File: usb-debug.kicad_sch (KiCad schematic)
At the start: 78 parts, among them IC15 TPS7A0518PDBVT, IC16 AP22653W6-7, IC7 HD3SS3220, J11 632723300011, Q1 PMV32UP, T6 BSS138APW, T7 BSS138APW

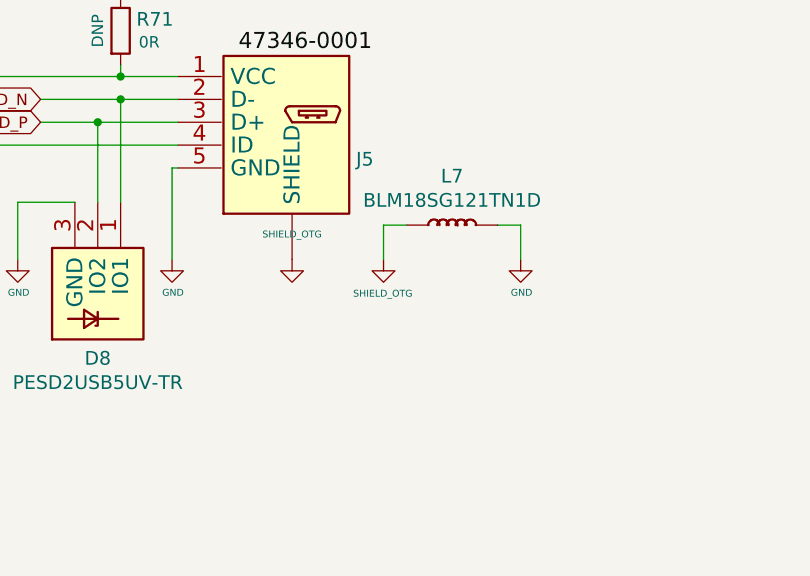
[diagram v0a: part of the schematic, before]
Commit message: Fixed schematic connection between USB OTG shield and L7
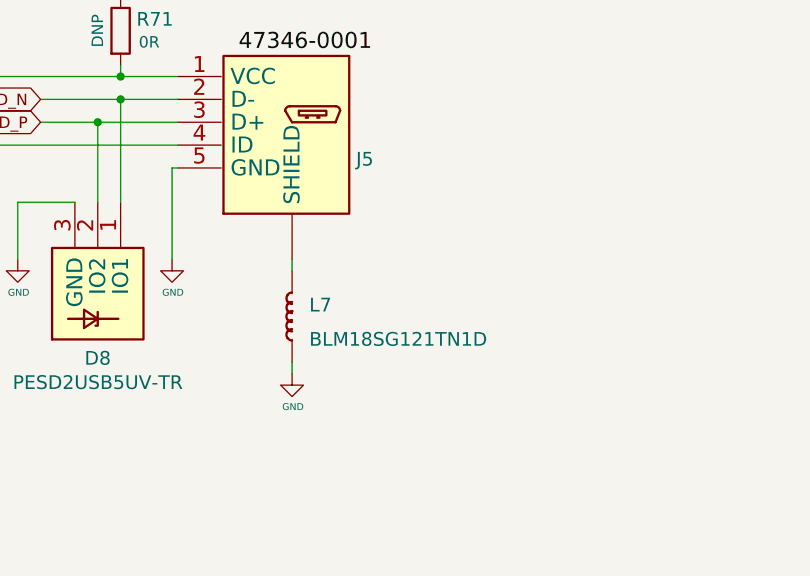
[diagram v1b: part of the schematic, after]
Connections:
- net GND: no longer J5.S (SHIELD), L7.2 (P)
- new net: J5.S (SHIELD), L7.2 (P)
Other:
- moved on the sheet: L7
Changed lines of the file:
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@@
     (stroke (width 0) (type default) (color 0 0 0 0))
   )
+  (wire (pts (xy 222.885 184.15) (xy 222.885 182.88))
+    (stroke (width 0) (type default) (color 0 0 0 0))
+  )
   (wire (pts (xy 192.405 165.1) (xy 192.405 171.45))
     (stroke (width 0) (type default) (color 0 0 0 0))
@@
     (stroke (width 0) (type default) (color 0 0 0 0))
   )
-  (wire (pts (xy 245.745 167.64) (xy 248.285 167.64))
-    (stroke (width 0) (type default) (color 0 0 0 0))
-  )
   (wire (pts (xy 151.13 50.8) (xy 151.13 58.42))
     (stroke (width 0) (type default) (color 0 0 0 0))
@@
     (stroke (width 0) (type default) (color 0 0 0 0))
   )
+  (wire (pts (xy 222.885 172.72) (xy 222.885 171.45))
+    (stroke (width 0) (type default) (color 0 0 0 0))
+  )
   (wire (pts (xy 222.25 261.62) (xy 222.25 258.445))
     (stroke (width 0) (type default) (color 0 0 0 0))
@@
     (stroke (width 0) (type default) (color 0 0 0 0))
   )
-  (wire (pts (xy 235.585 167.64) (xy 233.045 167.64))
-    (stroke (width 0) (type default) (color 0 0 0 0))
-  )
   (wire (pts (xy 290.195 86.995) (xy 290.195 59.055))
     (stroke (width 0) (type default) (color 0 0 0 0))
@@
     (stroke (width 0) (type default) (color 0 0 0 0))
   )
-  (wire (pts (xy 233.045 167.64) (xy 233.045 171.45))
-    (stroke (width 0) (type default) (color 0 0 0 0))
-  )
   (wire (pts (xy 102.235 244.475) (xy 102.235 227.965))
     (stroke (width 0) (type default) (color 0 0 0 0))
@@
     (stroke (width 0) (type default) (color 0 0 0 0))
   )
-  (wire (pts (xy 248.285 167.64) (xy 248.285 171.45))
-    (stroke (width 0) (type default) (color 0 0 0 0))
-  )
   (wire (pts (xy 42.545 165.1) (xy 42.545 166.37))
     (stroke (width 0) (type default) (color 0 0 0 0))
@@
     (pin "1")
   )
-  (symbol (lib_id "jetson-nano-baseboard:BLM18SG121TN1D") (at 240.665 167.64 0) (unit 1)
-    (in_bom yes) (on_board yes)
-    (property "Reference" "L7" (id 0) (at 240.665 162.2044 0)
-      (effects (font (size 1.524 1.524)))
+  (symbol (lib_id "jetson-nano-baseboard:BLM18SG121TN1D") (at 222.885 177.8 90) (unit 1)
+    (in_bom yes) (on_board yes) (fields_autoplaced)
+    (property "Reference" "L7" (id 0) (at 224.79 176.5298 90)
+      (effects (font (size 1.524 1.524)) (justify right))
     )
-    (property "Value" "BLM18SG121TN1D" (id 1) (at 240.665 164.8968 0)
-      (effects (font (size 1.524 1.524)))
+    (property "Value" "BLM18SG121TN1D" (id 1) (at 224.79 180.3398 90)
+      (effects (font (size 1.524 1.524)) (justify right))
     )
-    (property "Footprint" "jetson-nano-baseboard-footprints:0603" (id 2) (at 233.045 165.1 0)
+    (property "Footprint" "jetson-nano-baseboard-footprints:0603" (id 2) (at 220.345 185.42 0)
       (effects (font (size 1.524 1.524)) hide)
     )
-    (property "Datasheet" "" (id 3) (at 233.045 165.1 0)
+    (property "Datasheet" "" (id 3) (at 220.345 185.42 0)
       (effects (font (size 1.524 1.524)) hide)
     )
-    (property "Manufacturer" "Murata" (id 4) (at 154.305 380.8222 90)
+    (property "Manufacturer" "Murata" (id 4) (at 436.0672 264.16 90)
       (effects (font (size 1.524 1.524)) hide)
     )
-    (property "MPN" "BLM18SG121TN1D" (id 5) (at -665.3784 673.227 0)
+    (property "MPN" "BLM18SG121TN1D" (id 5) (at 728.472 1083.8434 0)
       (effects (font (size 1.27 1.27)) hide)
     )
@@
     (pin "1")
   )
-  (symbol (lib_id "jetson-nano-baseboard:GND") (at 222.885 171.45 0) (unit 1)
-    (in_bom yes) (on_board yes)
-    (property "Reference" "#SHIELD_OTG_02" (id 0) (at 222.885 167.894 0)
-      (effects (font (size 0.508 0.508)) hide)
-    )
-    (property "Value" "SHIELD_OTG" (id 1) (at 222.885 168.656 0)
-      (effects (font (size 0.762 0.762)))
-    )
-    (property "Footprint" "" (id 2) (at 222.885 171.45 0)
-      (effects (font (size 1.778 1.778)) hide)
-    )
-    (property "Datasheet" "" (id 3) (at 222.885 171.45 0)
-      (effects (font (size 1.778 1.778)) hide)
-    )
-    (pin "1")
-  )
-  (symbol (lib_id "jetson-nano-baseboard:GND") (at 248.285 171.45 0) (unit 1)
-    (in_bom yes) (on_board yes)
-    (property "Reference" "#GND_0107" (id 0) (at 248.285 171.45 0)
-      (effects (font (size 0.508 0.508)) hide)
-    )
-    (property "Value" "GND" (id 1) (at 248.3866 175.133 0)
-      (effects (font (size 0.762 0.762)))
-    )
-    (property "Footprint" "" (id 2) (at 248.285 171.45 0)
-      (effects (font (size 1.778 1.778)) hide)
-    )
-    (property "Datasheet" "" (id 3) (at 248.285 171.45 0)
-      (effects (font (size 1.778 1.778)) hide)
-    )
-    (pin "1")
-  )
-  (symbol (lib_id "jetson-nano-baseboard:GND") (at 233.045 171.45 0) (unit 1)
+  (symbol (lib_id "jetson-nano-baseboard:GND") (at 222.885 184.15 0) (unit 1)
     (in_bom yes) (on_board yes)
-    (property "Reference" "#SHIELD_OTG01" (id 0) (at 233.045 167.894 0)
+    (property "Reference" "#GND_0107" (id 0) (at 222.885 184.15 0)
       (effects (font (size 0.508 0.508)) hide)
     )
-    (property "Value" "SHIELD_OTG" (id 1) (at 232.9688 175.2346 0)
+    (property "Value" "GND" (id 1) (at 222.9866 187.833 0)
       (effects (font (size 0.762 0.762)))
     )
-    (property "Footprint" "" (id 2) (at 233.045 171.45 0)
+    (property "Footprint" "" (id 2) (at 222.885 184.15 0)
       (effects (font (size 1.778 1.778)) hide)
     )
-    (property "Datasheet" "" (id 3) (at 233.045 171.45 0)
+    (property "Datasheet" "" (id 3) (at 222.885 184.15 0)
       (effects (font (size 1.778 1.778)) hide)
     )

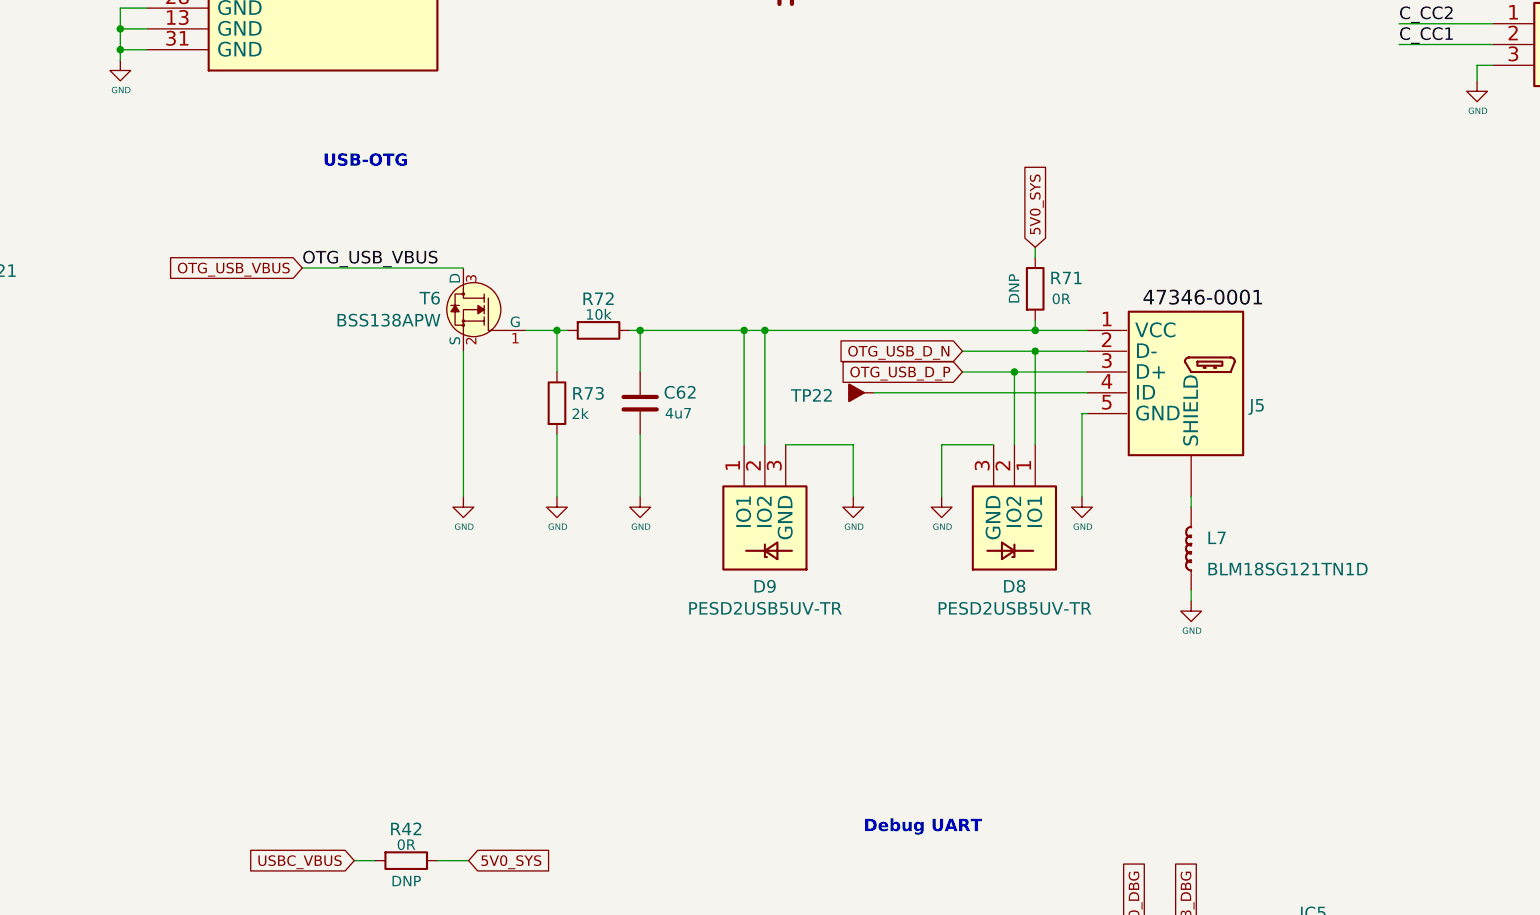
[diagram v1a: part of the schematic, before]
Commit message: Added USB OTG functionality
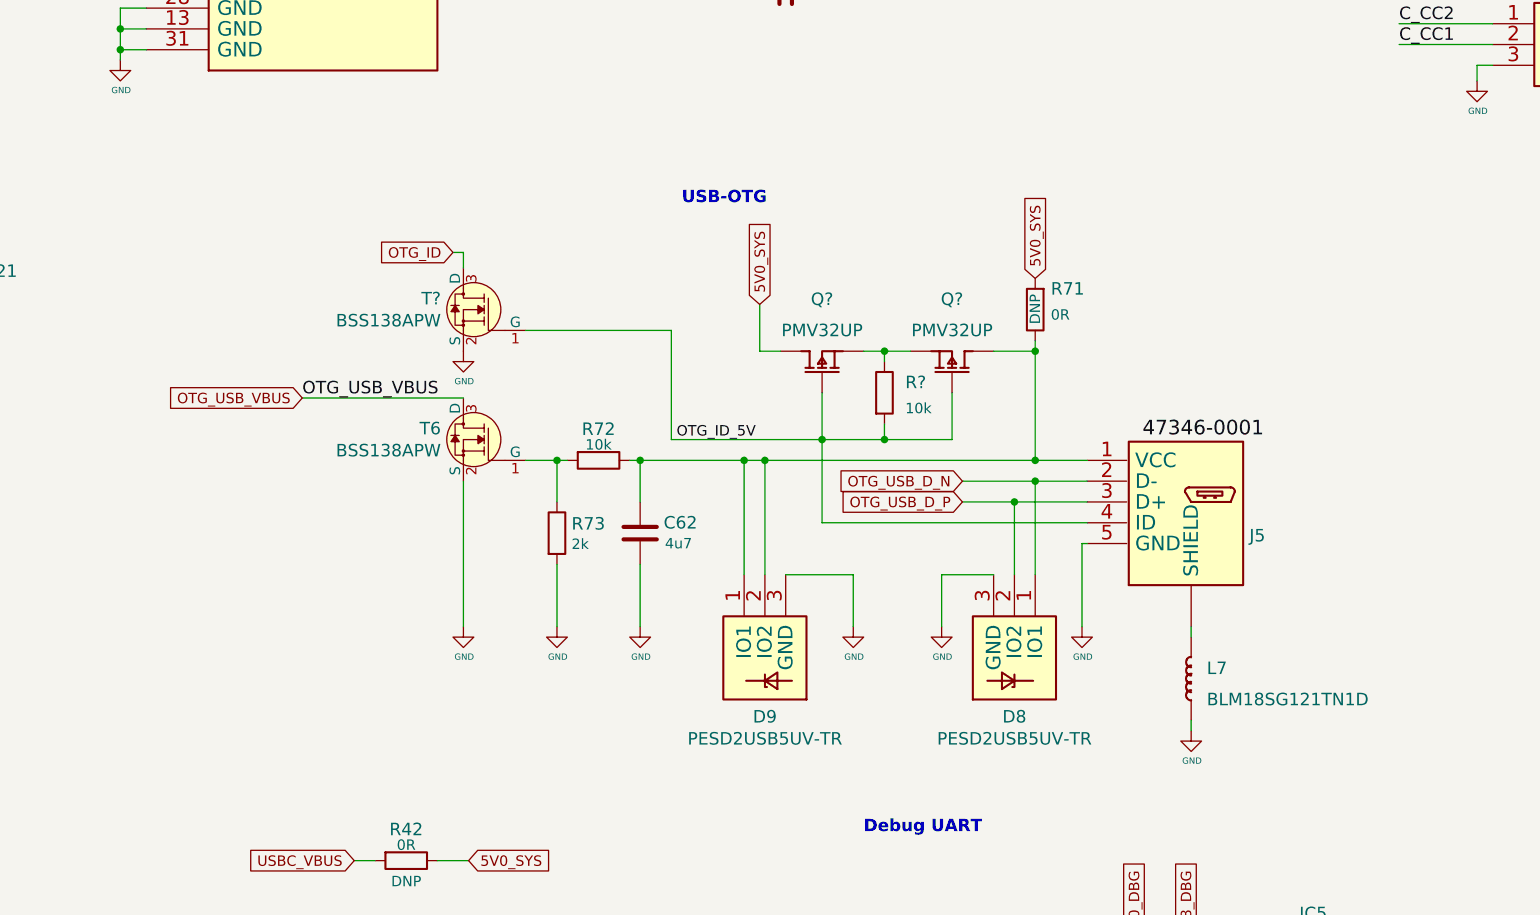
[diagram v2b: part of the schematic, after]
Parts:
- removed TP22: ~, jetson-nano-baseboard-footprints:TP-R-1.5, symbol jetson-nano-baseboard:Testpad
- added Q? (x2): PMV32UP, jetson-nano-baseboard-footprints:SOT-23s, symbol jetson-nano-baseboard:PMOS
- added R?: R_10k_0402, jetson-nano-baseboard-footprints:0402-res, symbol jetson-nano-baseboard:R_10k_0402
- added T?: BSS138APW, jetson-nano-baseboard-footprints:SC70-3, symbol jetson-nano-baseboard:BSS138APW
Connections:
- net 5V0_SYS: now also R71.2, Q?.3 (D); no longer R71.1
- net GND: now also T?.2 (S)
- net OTG_ID_5V: now reaches J5.4 (ID)
- net OTG_ID_5V: now also Q?.1 (G), Q?.1 (G), R?.2, T?.1 (G)
- net at C62.2, D9.1 (IO1), D9.2 (IO2)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: now also R71.1, Q?.3 (D); no longer R71.2
- new net: Q?.2 (S), Q?.2 (S), R?.1
- new net OTG_ID: T?.3 (D)
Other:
- moved on the sheet: C62, D8, D9, J5, L7, R71, R72, R73, T6

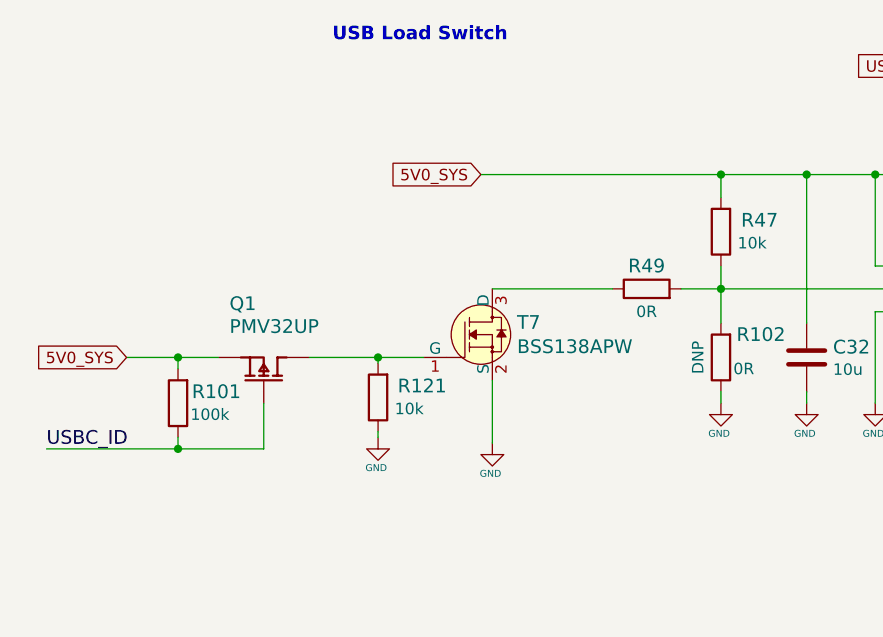
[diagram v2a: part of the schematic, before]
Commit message: Modified USBC ID logic
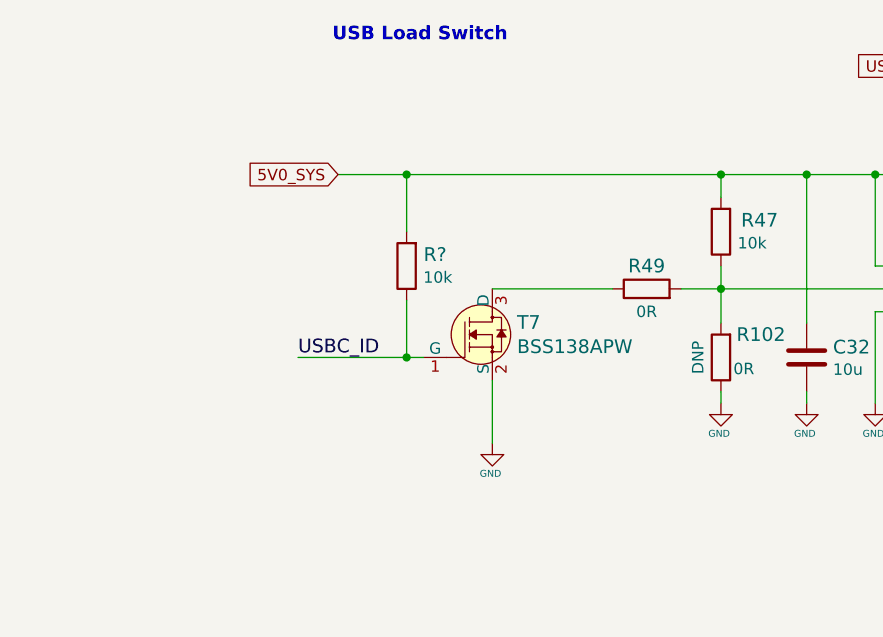
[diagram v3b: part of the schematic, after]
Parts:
- removed Q1: PMV32UP, jetson-nano-baseboard-footprints:SOT-23s, symbol jetson-nano-baseboard:PMOS
- removed R101: R_100k_0402, jetson-nano-baseboard-footprints:0402-res, symbol jetson-nano-baseboard:R_100k_0402
- removed R121: R_10k_0402, jetson-nano-baseboard-footprints:0402-res, symbol jetson-nano-baseboard:R_10k_0402
- added R?: R_10k_0402, jetson-nano-baseboard-footprints:0402-res, symbol jetson-nano-baseboard:R_10k_0402
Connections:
- net 5V0_SYS: now also R?.2
- net USBC_ID: now also T7.1 (G), R?.1

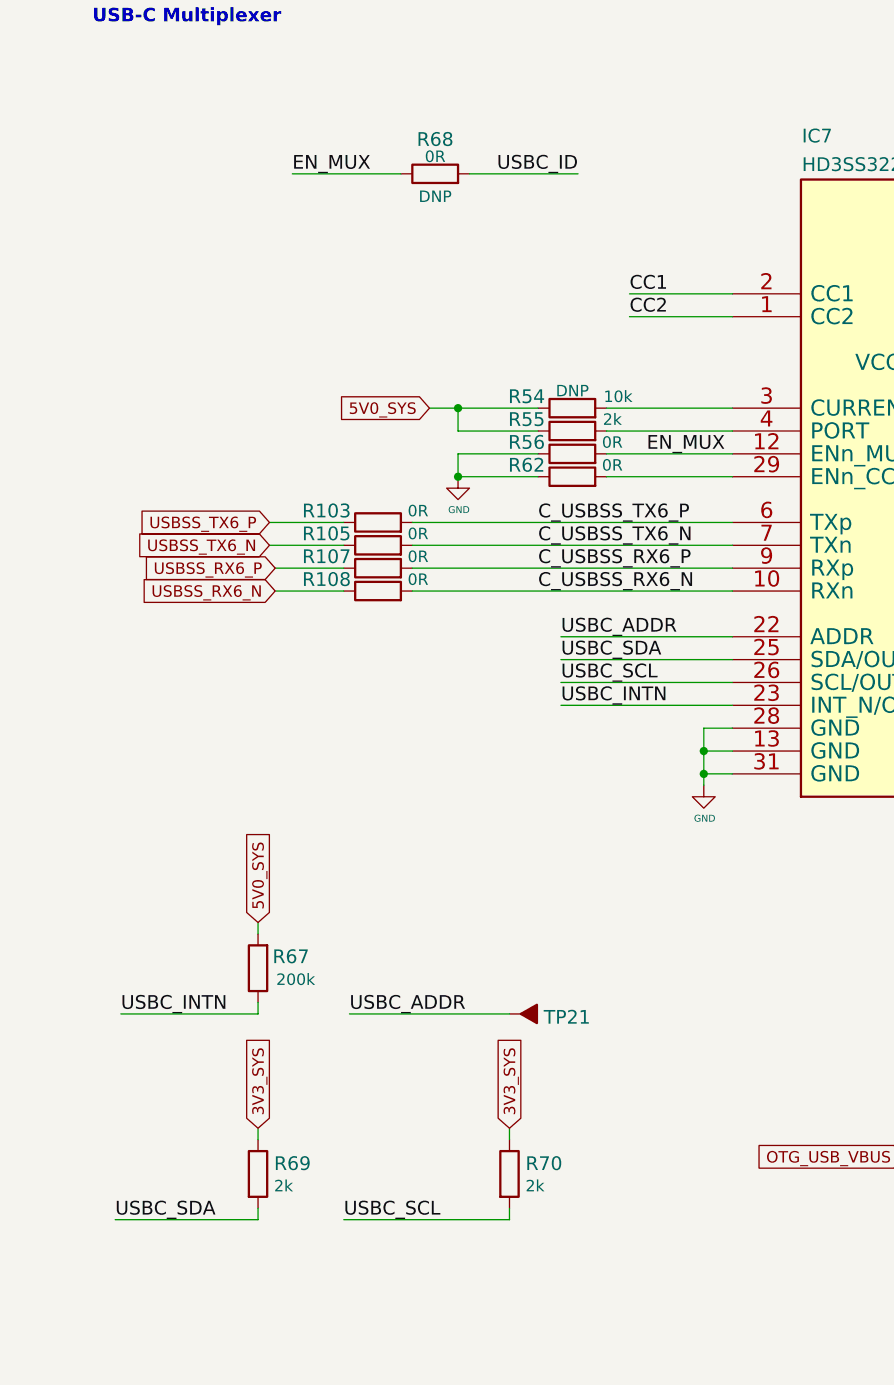
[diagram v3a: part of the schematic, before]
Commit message: Added OR resistors to connect IC7 to I2C bus
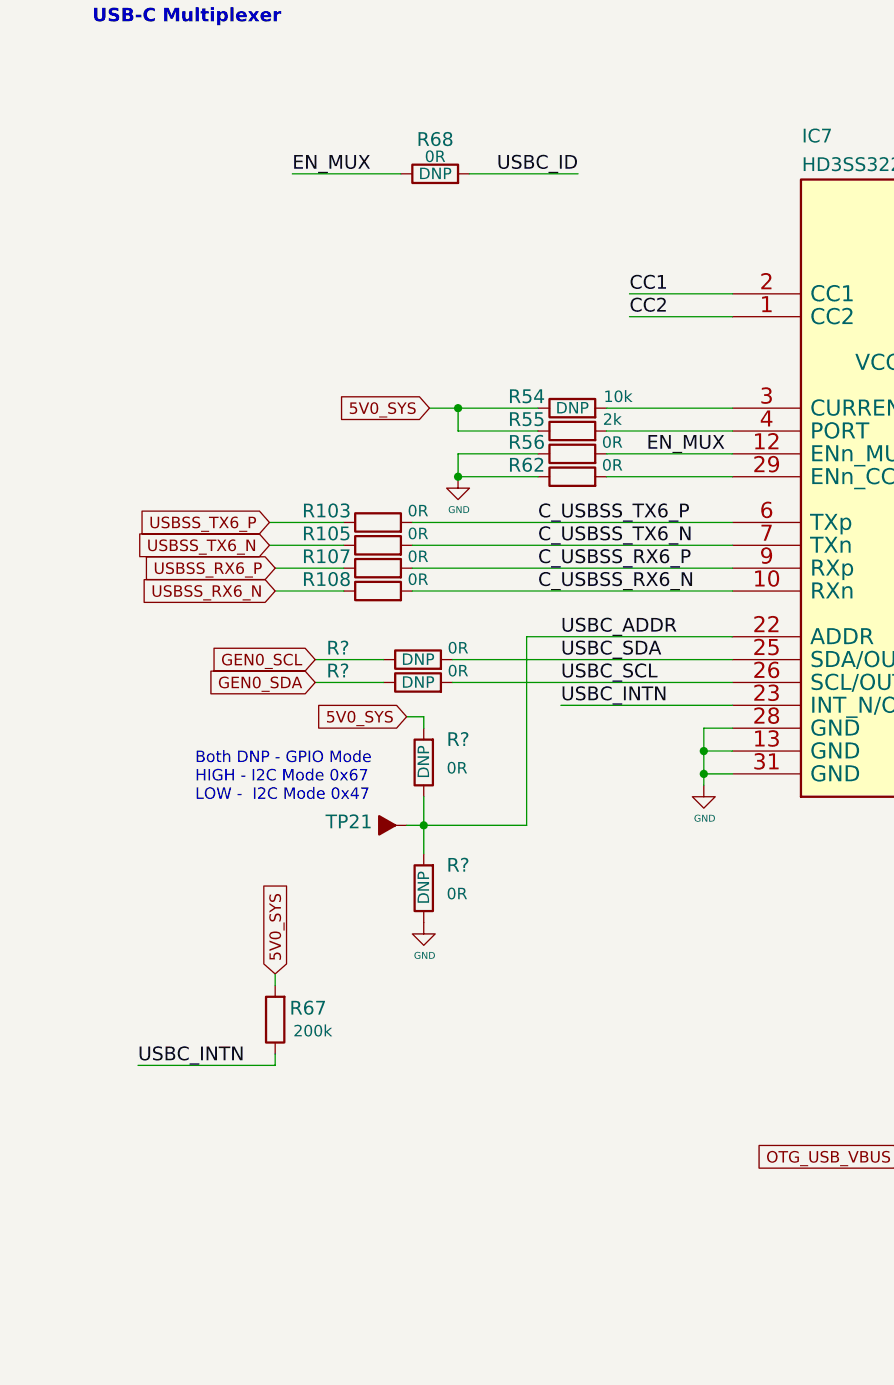
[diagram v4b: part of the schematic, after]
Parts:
- removed R69, R70: R_2k_0402, jetson-nano-baseboard-footprints:0402-res, symbol jetson-nano-baseboard:R_2k_0402
- added R? (x4): R_0R_0402, jetson-nano-baseboard-footprints:0402-res, symbol jetson-nano-baseboard:R_0R_0402
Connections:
- net 5V0_SYS: now also R?.2
- net GND: now also R?.1
- net USBC_ADDR: now also R?.1, R?.2
- net USBC_SCL: now also R?.2
- net USBC_SDA: now also R?.2
- new net GEN0_SCL: R?.1
- new net GEN0_SDA: R?.1
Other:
- note added: "Both DNP - GPIO Mode HIGH - I2C Mode 0x67 LOW - I2C Mode 0x47"
- moved on the sheet: R67, TP21
